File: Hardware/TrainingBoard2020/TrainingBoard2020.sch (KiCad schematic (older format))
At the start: 0 parts

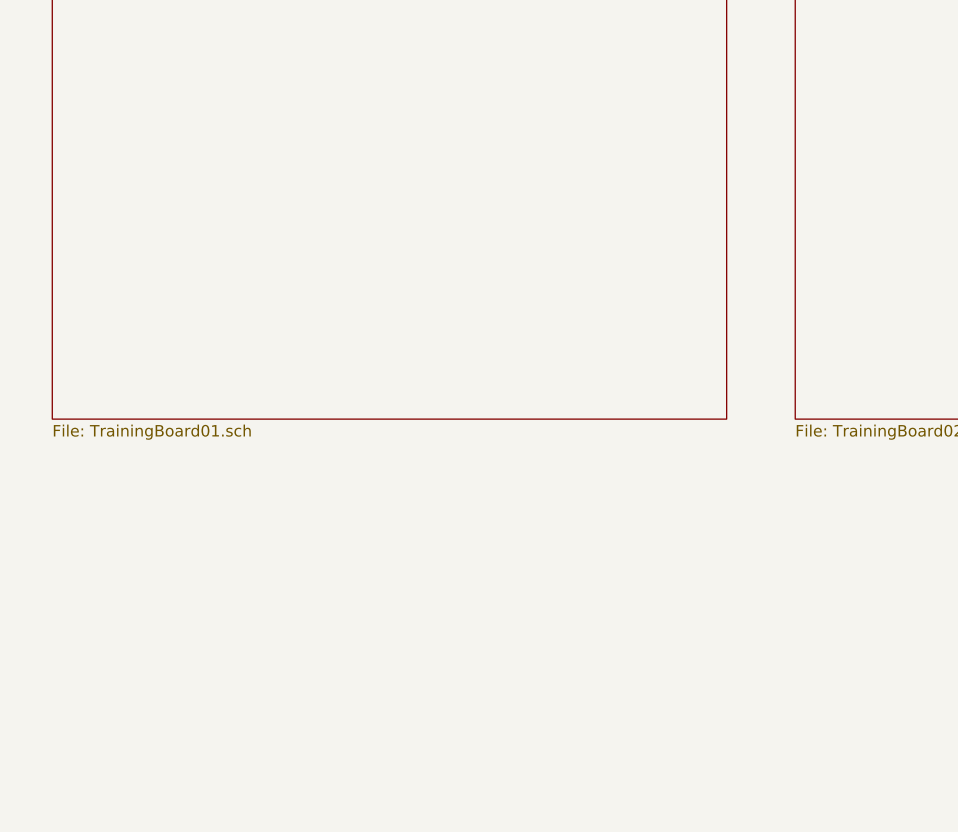
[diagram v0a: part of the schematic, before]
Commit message: Finished PCB layout
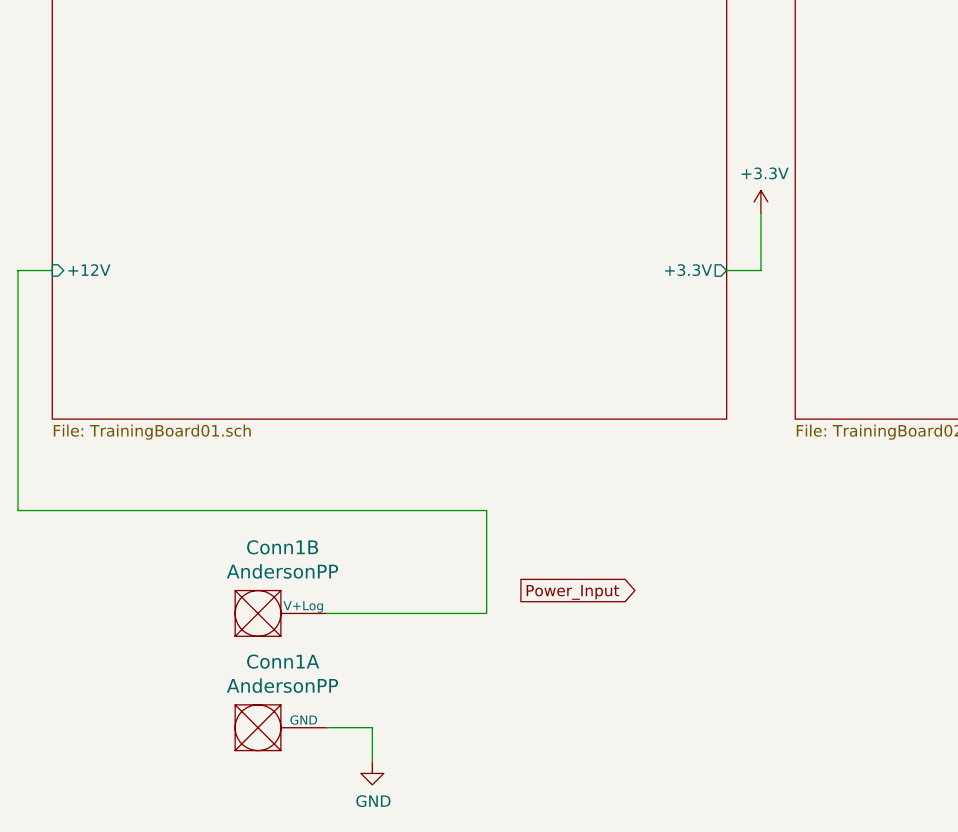
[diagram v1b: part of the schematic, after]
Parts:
- added Conn1: AndersonPP, MRDT_Connectors:Anderson_2_Horizontal_Side_by_Side, symbol MRDT_Connectors:AndersonPP
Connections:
- new net GND: Conn1.1 (GND)
- new net Power/+12V: Conn1.2 (V+Log)
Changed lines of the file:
@@
 F0 "Power" 50
 F1 "TrainingBoard01.sch" 50
+F2 "+12V" I L 750 3350 50
+F3 "+3.3V" O R 3700 3350 50
 $EndSheet
 $Sheet
@@
 F1 "TrainingBoard03.sch" 50
 $EndSheet
+$Comp
+L MRDT_Connectors:AndersonPP Conn?
+U 1 1 5F666172
+P 1550 5450
+AR Path="/5F567260/5F666172" Ref="Conn?"  Part="1"
+AR Path="/5F666172" Ref="Conn1"  Part="1"
+F 0 "Conn1" H 1758 5837 60  0000 C CNN
+F 1 "AndersonPP" H 1758 5731 60  0000 C CNN
+F 2 "MRDT_Connectors:Anderson_2_Horizontal_Side_by_Side" H 1400 4900 60  0001 C CNN
+F 3 "" H 1400 4900 60  0001 C CNN
+	1    1550 5450
+	1    0    0    -1
+$EndComp
+$Comp
+L MRDT_Connectors:AndersonPP Conn?
+U 2 1 5F666178
+P 1550 4950
+AR Path="/5F567260/5F666178" Ref="Conn?"  Part="2"
+AR Path="/5F666178" Ref="Conn1"  Part="2"
+F 0 "Conn1" H 1758 5337 60  0000 C CNN
+F 1 "AndersonPP" H 1758 5231 60  0000 C CNN
+F 2 "MRDT_Connectors:Anderson_2_Horizontal_Side_by_Side" H 1400 4400 60  0001 C CNN
+F 3 "" H 1400 4400 60  0001 C CNN
+	2    1550 4950
+	1    0    0    -1
+$EndComp
+$Comp
+L power:GND #PWR?
+U 1 1 5F66617E
+P 2150 5500
+AR Path="/5F567260/5F66617E" Ref="#PWR?"  Part="1"
+AR Path="/5F66617E" Ref="#PWR0101"  Part="1"
+F 0 "#PWR0101" H 2150 5250 50  0001 C CNN
+F 1 "GND" H 2155 5327 50  0000 C CNN
+F 2 "" H 2150 5500 50  0001 C CNN
+F 3 "" H 2150 5500 50  0001 C CNN
+	1    2150 5500
+	1    0    0    -1
+$EndComp
+Wire Wire Line
+	1950 5350 2150 5350
+Wire Wire Line
+	2150 5350 2150 5500
+Text GLabel 2800 4750 2    49   Output ~ 0
+Power_Input
+Wire Wire Line
+	2650 4850 2650 4400
+Wire Wire Line
+	2650 4400 600  4400
+Wire Wire Line
+	600  4400 600  3350
+Wire Wire Line
+	600  3350 750  3350
+Wire Wire Line
+	1950 4850 2650 4850
+$Comp
+L power:+3.3V #PWR0102
+U 1 1 5F6685E1
+P 3850 3100
+F 0 "#PWR0102" H 3850 2950 50  0001 C CNN
+F 1 "+3.3V" H 3865 3273 50  0000 C CNN
+F 2 "" H 3850 3100 50  0001 C CNN
+F 3 "" H 3850 3100 50  0001 C CNN
+	1    3850 3100
+	1    0    0    -1
+$EndComp
+Wire Wire Line
+	3700 3350 3850 3350
+Wire Wire Line
+	3850 3350 3850 3100
 $EndSCHEMATC
